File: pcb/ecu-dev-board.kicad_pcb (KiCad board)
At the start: 4 copper layers, 99.9 x 99.9 mm, 258 parts, among them IC201 MAX9924UAUB+, IC401 74HC14D-Q100,118, IC601 UCC28910DR, IC701 UCC27624DR, J101 MX23A18NF1, J102 39-30-1020, K501 Relay, Q201 MMBT2222A, Q501 MMBT2222A, Q502 MMBTA55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

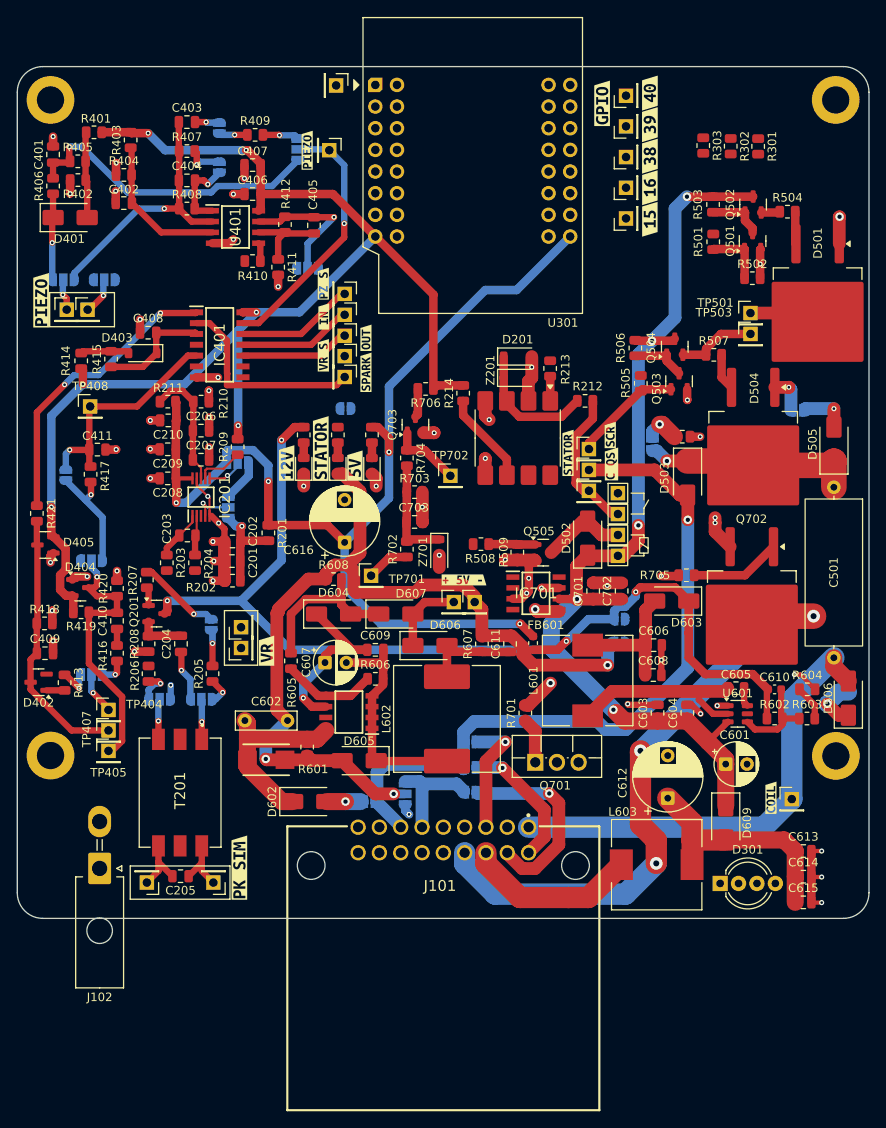
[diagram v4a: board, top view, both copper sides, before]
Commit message: routed GPIOs
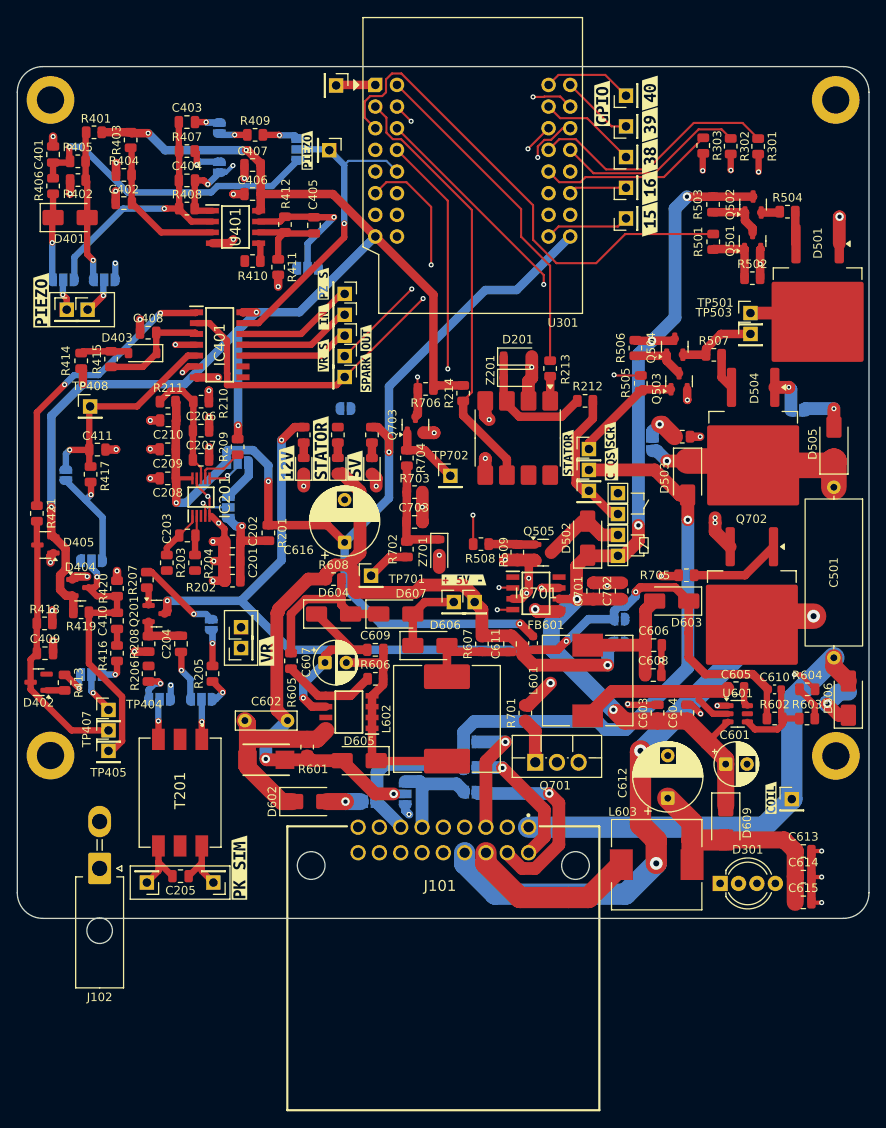
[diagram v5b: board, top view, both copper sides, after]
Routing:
- net Net-(D301-RA): track 0.00 -> 89.3 mm, vias 0 -> 1
- net Net-(D301-GA): track 0.00 -> 87.6 mm, vias 0 -> 1
- net Net-(D301-BA): track 0.00 -> 86.4 mm, vias 0 -> 1
- net MAP_SW: track 0.00 -> 78.4 mm
- net ENABLE_QS: track 0.00 -> 76.7 mm
- net PIEZO+: track 4.42 -> 73.0 mm
- net PIEZO-: track 3.71 -> 65.9 mm
- net POWER_FET: track 0.00 -> 61.2 mm, vias 0 -> 2
- net T_CUT: track 0.00 -> 60.0 mm, vias 0 -> 2
- net SCR_QS_KS: track 0.00 -> 59.8 mm
- net RELAY_QS: track 0.00 -> 49.9 mm, vias 0 -> 2
- net T_RPM: track 3.38 -> 48.1 mm, vias 0 -> 2
- net SCR: track 0.00 -> 42.6 mm, vias 0 -> 2
- net COIL_SPARK_OUT: track 10.8 -> 51.0 mm
- net SSR_IN: track 0.00 -> 39.8 mm
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
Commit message: fixed DRC errors
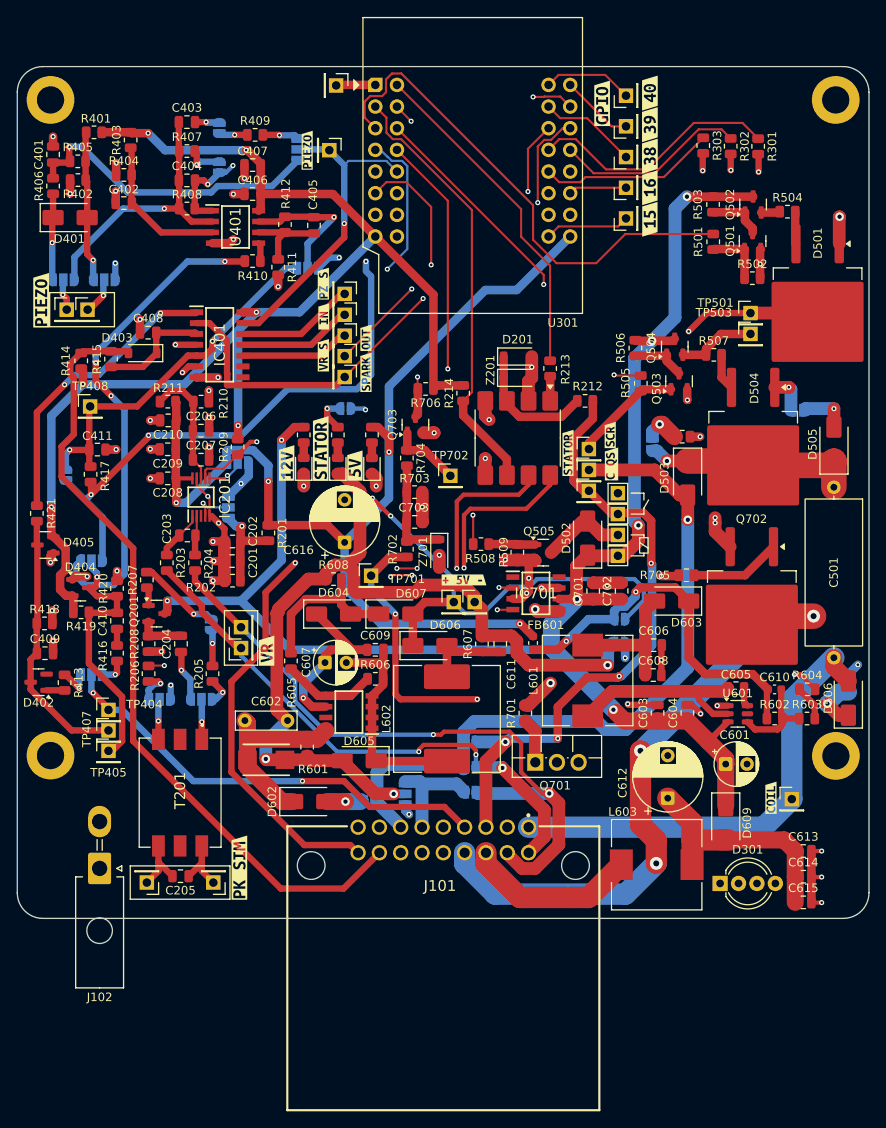
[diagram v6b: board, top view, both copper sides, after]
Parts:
- moved C611 1.15 mm to (209.6, 103.7)
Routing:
- net TPS: track 0.00 -> 102.9 mm, vias 0 -> 2
- net VR-: track 23.0 -> 120.2 mm, vias 1 -> 3
- net PICKUP_SIM_IN-: track 0.00 -> 95.0 mm, vias 0 -> 3
- net VR+: track 15.6 -> 106.0 mm, vias 1 -> 4
- net DIGITAL_QS_IN: track 5.72 -> 93.8 mm
- net PICKUP_SIM_IN+: track 4.25 -> 87.4 mm, vias 1 -> 3
- net KILL_SWITCH: track 8.30 -> 86.9 mm, vias 0 -> 1
- net /Sensor/FILTER: track 13.6 -> 72.2 mm, vias 1 -> 4
- net Net-(D606-K): track 9.08 -> 67.3 mm, vias 0 -> 3
- net /Sensor/OPAMP: track 0.00 -> 57.9 mm, vias 0 -> 3
- net SPARK: track 4.98 -> 52.4 mm, vias 1 -> 2
- net T_COIL: track 80.4 -> 126.9 mm, vias 3 -> 5
- net COIL_QS: track 31.1 -> 74.4 mm, vias 1 -> 4
- net VR_SQUARE: track 39.7 -> 57.1 mm, vias 2 -> 3
- net /Sensor/COUP_SPARK: track 26.9 -> 43.3 mm, vias 1 -> 2
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
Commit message: components updates
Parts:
- R207, R605, R606, R608: footprint Resistor_SMD:R_0805_2012Metric -> Resistor_SMD:R_0603_1608Metric
- R301, R302, R303: value 180 -> 200
- R405: value 2M -> 1M
- R418: value 680k -> 470k

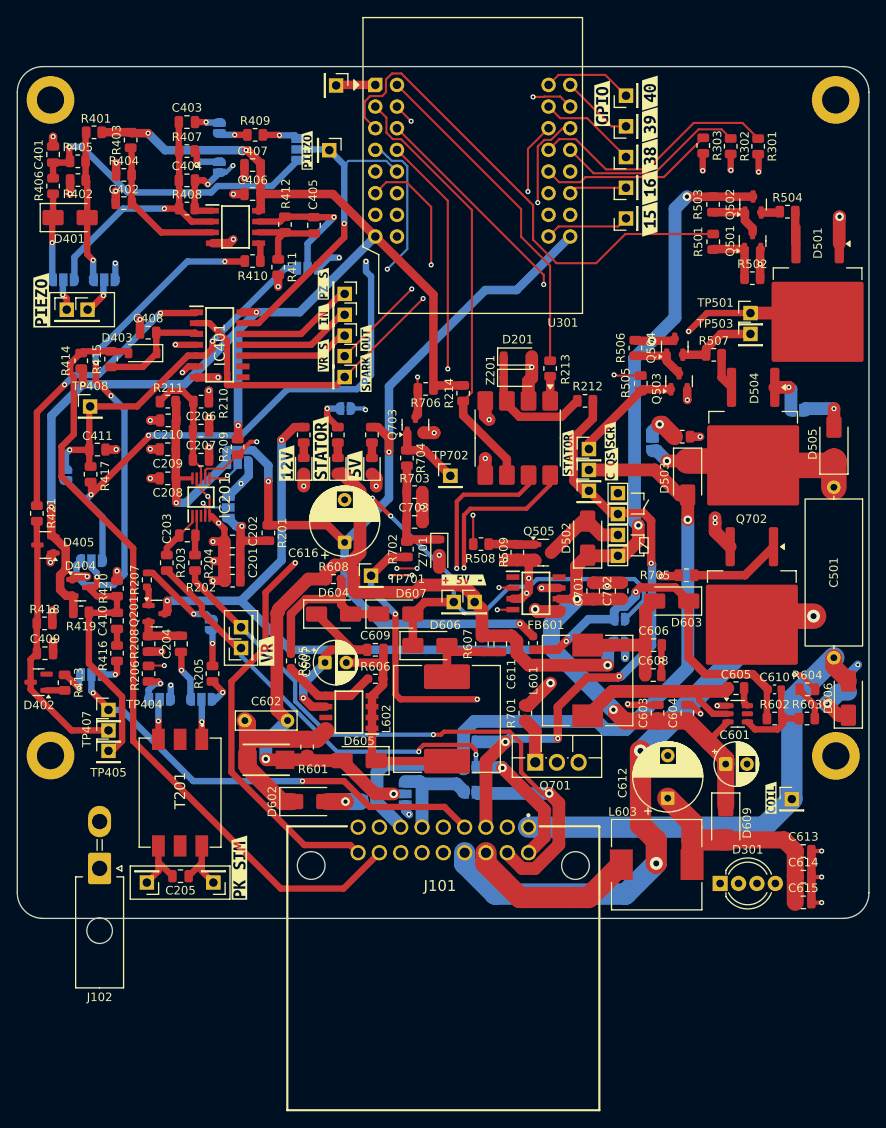
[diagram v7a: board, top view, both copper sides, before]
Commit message: swapped ADC with digital pins
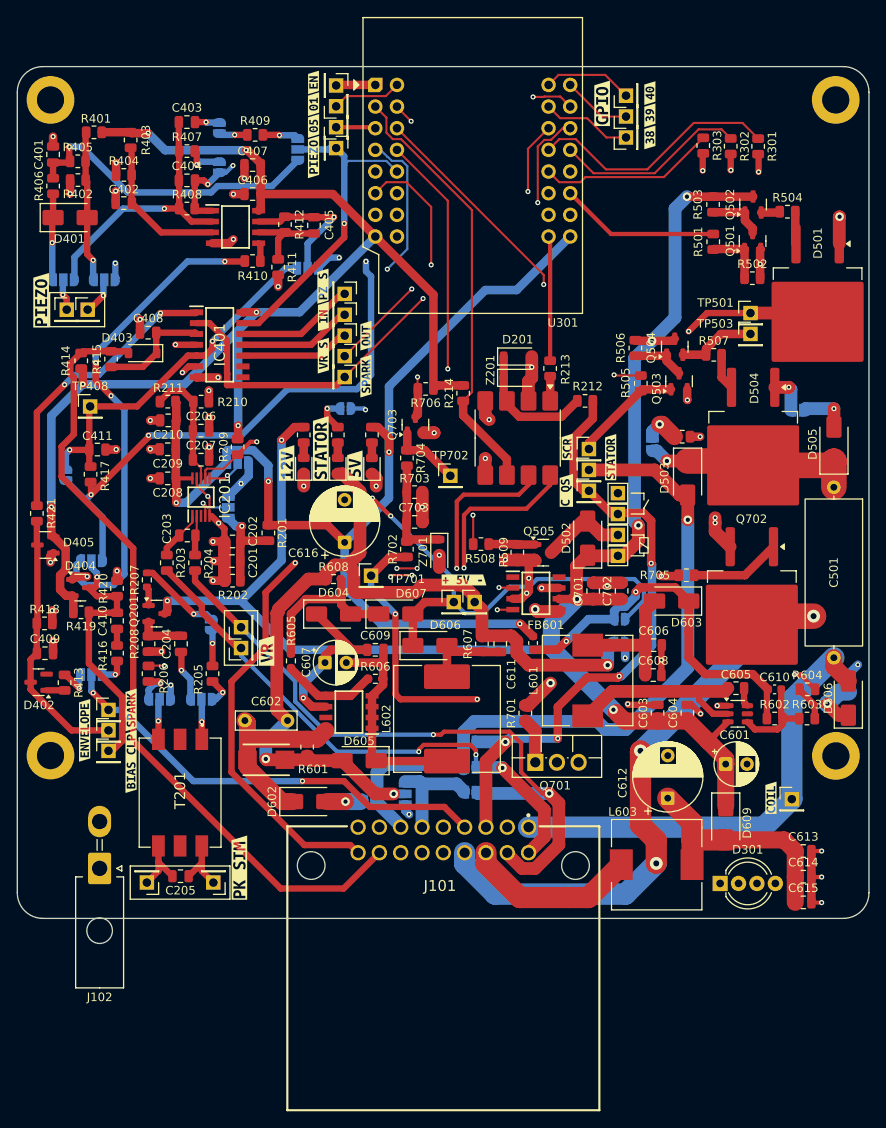
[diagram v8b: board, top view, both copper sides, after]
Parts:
- removed kibuzzard-68DD8689: G***, kibuzzard-68DD8689
- removed kibuzzard-68DD8695: G***, kibuzzard-68DD8695
- removed kibuzzard-68DD86A0: G***, kibuzzard-68DD86A0
- removed kibuzzard-68DD86A6: G***, kibuzzard-68DD86A6
- removed kibuzzard-68DD86AD: G***, kibuzzard-68DD86AD
- removed kibuzzard-68E56F81: G***, kibuzzard-68E56F81
- removed kibuzzard-68E56F97: G***, kibuzzard-68E56F97
- removed kibuzzard-68E56FA3: G***, kibuzzard-68E56FA3
- removed kibuzzard-68E56FAD: G***, kibuzzard-68E56FAD
- removed kibuzzard-68E571D7: G***, kibuzzard-68E571D7
- removed kibuzzard-68E57203: G***, kibuzzard-68E57203
- added kibuzzard-68EB72B9: G***, kibuzzard-68EB72B9, F.Cu at (227.1, 39.1)
- added kibuzzard-68EB72C7: G***, kibuzzard-68EB72C7, F.Cu at (227.1, 41.7)
- added kibuzzard-68EB72CC: G***, kibuzzard-68EB72CC, F.Cu at (227.1, 44.3)
- added kibuzzard-68EB72E2: G***, kibuzzard-68EB72E2, F.Cu at (187.7, 37.9)
- added kibuzzard-68EB72EA: G***, kibuzzard-68EB72EA, F.Cu at (187.7, 40.4)
- added kibuzzard-68EB72EE: G***, kibuzzard-68EB72EE, F.Cu at (187.7, 43.0)
- added kibuzzard-68EB72F2: G***, kibuzzard-68EB72F2, F.Cu at (187.7, 46.6)
- added kibuzzard-68EB7325: G***, kibuzzard-68EB7325, F.Cu at (188.8, 61.8)
- added kibuzzard-68EB732B: G***, kibuzzard-68EB732B, F.Cu at (188.8, 65.3)
- added kibuzzard-68EB7336: G***, kibuzzard-68EB7336, F.Cu at (188.8, 69.9)
- added kibuzzard-68EB733C: G***, kibuzzard-68EB733C, F.Cu at (193.8, 67.5)
- added kibuzzard-68EB7341: G***, kibuzzard-68EB7341, F.Cu at (193.8, 72.3)
- added kibuzzard-68EB73A6: G***, kibuzzard-68EB73A6, F.Cu at (166.2, 111.5)
- added kibuzzard-68EB7408: G***, kibuzzard-68EB7408, F.Cu at (166.2, 117.5)
- added kibuzzard-68EB7423: G***, kibuzzard-68EB7423, F.Cu at (160.8, 113.8)
- C610: value 82p -> 100p
- moved TP303 35.6 mm to (190.3, 43.1)
- moved TP302 35.3 mm to (190.3, 40.6)
- moved kibuzzard-68E57016 6.14 mm to (217.3, 85.7)
- moved kibuzzard-68E56FCB 5.24 mm to (217.4, 80.6)
- moved kibuzzard-68E56FD6 5.02 mm to (222.5, 81.8)
- moved TP304 2.30 mm to (224.3, 44.3)
- moved TP305 1.15 mm to (224.3, 41.9)
- moved TP403 0.84 mm to (190.3, 45.5)
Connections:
- TP302 pad 1: Net-(U301-XTAL_32K_N) -> Net-(U301-GPIO1)
- TP303 pad 1: Net-(U301-XTAL_32K_P) -> Net-(U301-GPIO5)
- U301 pad 11: Net-(U301-XTAL_32K_N) -> SCR_QS_KS
- U301 pad 17: SSR_IN -> Net-(U301-GPIO1)
- U301 pad 25: Net-(U301-XTAL_32K_P) -> SSR_IN
- U301 pad 3: SCR_QS_KS -> Net-(U301-GPIO5)
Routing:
- net SCR_QS_KS: track 59.8 -> 18.8 mm
- net SSR_IN: track 39.8 -> 14.6 mm
- net Net-(U301-XTAL_32K_P): track 9.96 -> 0.00 mm
- net Net-(U301-GPIO1): track 0.00 -> 8.18 mm
- net Net-(U301-XTAL_32K_N): track 6.81 -> 0.00 mm
- net Net-(U301-GPIO5): track 0.00 -> 4.65 mm
- net Net-(U301-GPIO38): track 11.5 -> 10.6 mm
- net PIEZO: track 37.6 -> 38.4 mm
